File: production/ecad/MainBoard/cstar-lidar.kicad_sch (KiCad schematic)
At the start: 3 parts, among them J1 532610771, J2 Conn_01x02_Pin, J3 Conn_01x02_Pin

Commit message: rereferenced
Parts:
- renumbered J2 to J5, J3 to J6, J1 to J7
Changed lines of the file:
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@@
   (symbol (lib_id "power:GND") (at 133.35 86.36 0) (unit 1)
     (in_bom yes) (on_board yes) (dnp no) (fields_autoplaced)
-    (property "Reference" "#PWR06" (at 133.35 92.71 0)
+    (property "Reference" "#PWR032" (at 133.35 92.71 0)
       (effects (font (size 1.27 1.27)) hide)
     )
@@
     (pin "1")
     (instances
+      (project "CSTAR"
+        (path "/cd9fa943-c6eb-468b-990c-ea873c442553/3e924a05-61af-4a8a-bc82-0b26814a19c7"
+          (reference "#PWR032") (unit 1)
+        )
+      )
       (project "cstar-lidar"
         (path "/f4254b98-3297-4812-862b-6470cd23e6be"
@@
   (symbol (lib_id "power:GND") (at 118.11 69.85 0) (unit 1)
     (in_bom yes) (on_board yes) (dnp no)
-    (property "Reference" "#PWR04" (at 118.11 76.2 0)
+    (property "Reference" "#PWR027" (at 118.11 76.2 0)
       (effects (font (size 1.27 1.27)) hide)
     )
@@
       (project "CSTAR"
         (path "/cd9fa943-c6eb-468b-990c-ea873c442553/3e924a05-61af-4a8a-bc82-0b26814a19c7"
+          (reference "#PWR027") (unit 1)
+        )
+      )
+      (project "cstar-lidar"
+        (path "/f4254b98-3297-4812-862b-6470cd23e6be"
           (reference "#PWR04") (unit 1)
         )
       )
-      (project "cstar-lidar"
-        (path "/f4254b98-3297-4812-862b-6470cd23e6be"
-          (reference "#PWR04") (unit 1)
-        )
-      )
     )
   )
   (symbol (lib_id "power:+5V") (at 129.54 60.96 90) (unit 1)
     (in_bom yes) (on_board yes) (dnp no) (fields_autoplaced)
-    (property "Reference" "#PWR03" (at 133.35 60.96 0)
+    (property "Reference" "#PWR029" (at 133.35 60.96 0)
       (effects (font (size 1.27 1.27)) hide)
     )
@@
       (project "CSTAR"
         (path "/cd9fa943-c6eb-468b-990c-ea873c442553/3e924a05-61af-4a8a-bc82-0b26814a19c7"
+          (reference "#PWR029") (unit 1)
+        )
+      )
+      (project "cstar-lidar"
+        (path "/f4254b98-3297-4812-862b-6470cd23e6be"
           (reference "#PWR03") (unit 1)
         )
       )
-      (project "cstar-lidar"
-        (path "/f4254b98-3297-4812-862b-6470cd23e6be"
-          (reference "#PWR03") (unit 1)
-        )
-      )
     )
   )
   (symbol (lib_id "power:GND") (at 128.27 82.55 0) (unit 1)
     (in_bom yes) (on_board yes) (dnp no) (fields_autoplaced)
-    (property "Reference" "#PWR07" (at 128.27 88.9 0)
+    (property "Reference" "#PWR028" (at 128.27 88.9 0)
       (effects (font (size 1.27 1.27)) hide)
     )
@@
     (pin "1")
     (instances
+      (project "CSTAR"
+        (path "/cd9fa943-c6eb-468b-990c-ea873c442553/3e924a05-61af-4a8a-bc82-0b26814a19c7"
+          (reference "#PWR028") (unit 1)
+        )
+      )
       (project "cstar-lidar"
         (path "/f4254b98-3297-4812-862b-6470cd23e6be"
@@
   (symbol (lib_id "power:GND") (at 113.03 68.58 0) (unit 1)
     (in_bom yes) (on_board yes) (dnp no) (fields_autoplaced)
-    (property "Reference" "#PWR02" (at 113.03 74.93 0)
+    (property "Reference" "#PWR026" (at 113.03 74.93 0)
       (effects (font (size 1.27 1.27)) hide)
     )
@@
     (pin "1")
     (instances
+      (project "CSTAR"
+        (path "/cd9fa943-c6eb-468b-990c-ea873c442553/3e924a05-61af-4a8a-bc82-0b26814a19c7"
+          (reference "#PWR026") (unit 1)
+        )
+      )
       (project "cstar-lidar"
         (path "/f4254b98-3297-4812-862b-6470cd23e6be"
@@
   (symbol (lib_id "532610771:532610771") (at 147.32 71.12 0) (unit 1)
     (in_bom yes) (on_board yes) (dnp no) (fields_autoplaced)
-    (property "Reference" "J1" (at 156.21 71.12 0)
+    (property "Reference" "J7" (at 156.21 71.12 0)
       (effects (font (size 1.27 1.27)) (justify left))
     )
@@
       (project "CSTAR"
         (path "/cd9fa943-c6eb-468b-990c-ea873c442553/3e924a05-61af-4a8a-bc82-0b26814a19c7"
-          (reference "J1") (unit 1)
+          (reference "J7") (unit 1)
         )
       )
@@
   (symbol (lib_id "power:+3V3") (at 129.54 63.5 90) (unit 1)
     (in_bom yes) (on_board yes) (dnp no)
-    (property "Reference" "#PWR01" (at 133.35 63.5 0)
+    (property "Reference" "#PWR030" (at 133.35 63.5 0)
       (effects (font (size 1.27 1.27)) hide)
     )
@@
       (project "CSTAR"
         (path "/cd9fa943-c6eb-468b-990c-ea873c442553/3e924a05-61af-4a8a-bc82-0b26814a19c7"
-          (reference "#PWR01") (unit 1)
+          (reference "#PWR030") (unit 1)
         )
       )
@@
   (symbol (lib_id "Connector:Conn_01x02_Pin") (at 101.6 73.66 270) (unit 1)
     (in_bom yes) (on_board yes) (dnp no)
-    (property "Reference" "J2" (at 93.98 68.58 90)
+    (property "Reference" "J5" (at 93.98 68.58 90)
       (effects (font (size 1.27 1.27)) (justify left))
     )
@@
     (pin "2")
     (instances
+      (project "CSTAR"
+        (path "/cd9fa943-c6eb-468b-990c-ea873c442553/3e924a05-61af-4a8a-bc82-0b26814a19c7"
+          (reference "J5") (unit 1)
+        )
+      )
       (project "cstar-lidar"
         (path "/f4254b98-3297-4812-862b-6470cd23e6be"
@@
   (symbol (lib_id "Connector:Conn_01x02_Pin") (at 102.87 80.01 270) (unit 1)
     (in_bom yes) (on_board yes) (dnp no)
-    (property "Reference" "J3" (at 96.52 87.63 90)
+    (property "Reference" "J6" (at 96.52 87.63 90)
       (effects (font (size 1.27 1.27)) (justify left))
     )
@@
     (pin "2")
     (instances
+      (project "CSTAR"
+        (path "/cd9fa943-c6eb-468b-990c-ea873c442553/3e924a05-61af-4a8a-bc82-0b26814a19c7"
+          (reference "J6") (unit 1)
+        )
+      )
       (project "cstar-lidar"
         (path "/f4254b98-3297-4812-862b-6470cd23e6be"
@@
   (symbol (lib_id "power:+5V") (at 129.54 71.12 90) (unit 1)
     (in_bom yes) (on_board yes) (dnp no) (fields_autoplaced)
-    (property "Reference" "#PWR05" (at 133.35 71.12 0)
+    (property "Reference" "#PWR031" (at 133.35 71.12 0)
       (effects (font (size 1.27 1.27)) hide)
     )
@@
       (project "CSTAR"
         (path "/cd9fa943-c6eb-468b-990c-ea873c442553/3e924a05-61af-4a8a-bc82-0b26814a19c7"
-          (reference "#PWR05") (unit 1)
-        )
-      )
+          (reference "#PWR031") (unit 1)
+        )
+      )

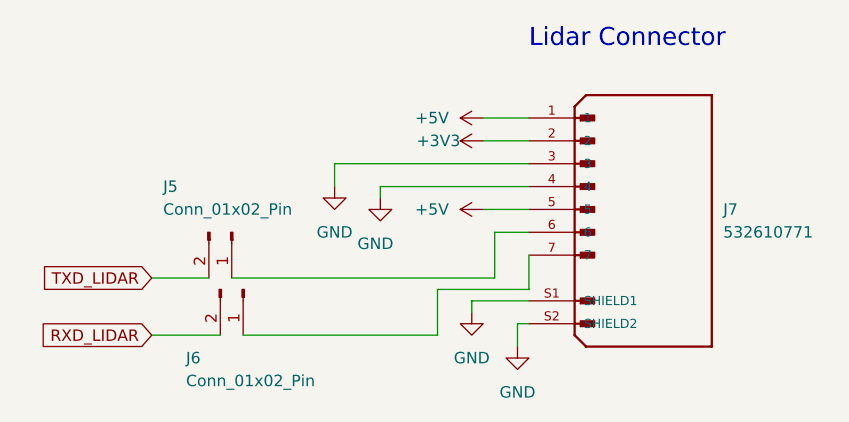
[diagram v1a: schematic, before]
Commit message: Changed connector pin
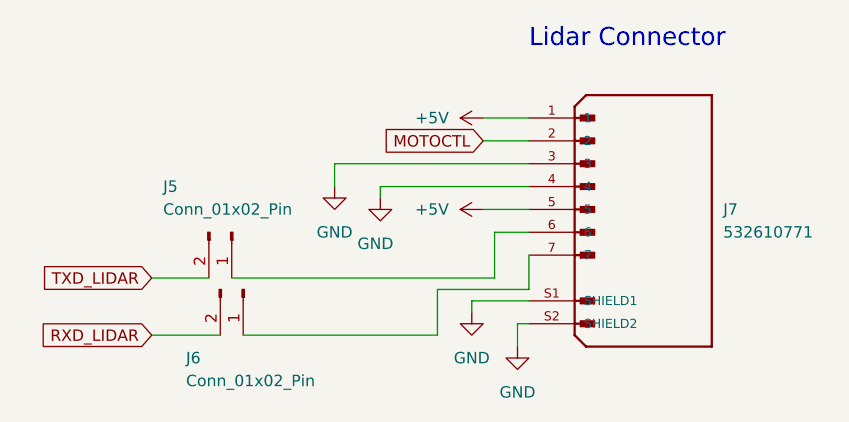
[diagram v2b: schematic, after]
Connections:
- net +3V3 renamed MOTOCTL
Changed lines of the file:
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@@
     (effects (font (size 2 2)) (justify left bottom))
+  )
+  (global_label "MOTOCTL" (shape input) (at 129.54 63.5 180) (fields_autoplaced)
+    (effects (font (size 1.27 1.27)) (justify right))
+    (property "Intersheetrefs" "${INTERSHEET_REFS}" (at 118.2091 63.5 0)
+      (effects (font (size 1.27 1.27)) (justify right) hide)
+    )
   )
   (global_label "RXD_LIDAR" (shape input) (at 92.71 85.09 180) (fields_autoplaced)
@@
         )
       )
-    )
-  )
-  (symbol (lib_id "power:+3V3") (at 129.54 63.5 90) (unit 1)
-    (in_bom yes) (on_board yes) (dnp no)
-    (property "Reference" "#PWR030" (at 133.35 63.5 0)
-      (effects (font (size 1.27 1.27)) hide)
-    )
-    (property "Value" "+3V3" (at 127 63.5 90)
-      (effects (font (size 1.27 1.27)) (justify left))
-    )
-    (property "Footprint" "" (at 129.54 63.5 0)
-      (effects (font (size 1.27 1.27)) hide)
-    )
-    (property "Datasheet" "" (at 129.54 63.5 0)
-      (effects (font (size 1.27 1.27)) hide)
-    )
-    (pin "1")
-    (instances
-      (project "CSTAR"
-        (path "/cd9fa943-c6eb-468b-990c-ea873c442553/3e924a05-61af-4a8a-bc82-0b26814a19c7"
-          (reference "#PWR030") (unit 1)
-        )
-      )
-      (project "cstar-lidar"
-        (path "/f4254b98-3297-4812-862b-6470cd23e6be"
-          (reference "#PWR01") (unit 1)
-        )
-      )
